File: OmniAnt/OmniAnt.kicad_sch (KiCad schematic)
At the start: 46 parts, among them J101 Connector, USB-TYPE-C-16P, J102 Conn_01x02_Pin, J103 Conn_01x04_Pin, J104 XT30PW-M, J105 XT30PW-M, J106 XT30PW-M, J107 XT30PW-M, J108 Conn_01x01, J109 Conn_01x01, J110 Conn_01x01, J111 Conn_01x01, J112 Conn_01x01, J113 Conn_01x01, J114 Conn_01x01, J115 Conn_01x01, J116 Conn_01x01, J117 Conn_01x01, U101 USBLC6-2P6, U102 TPSM53603RDA, U103 ESP32-S3-WROOM-1

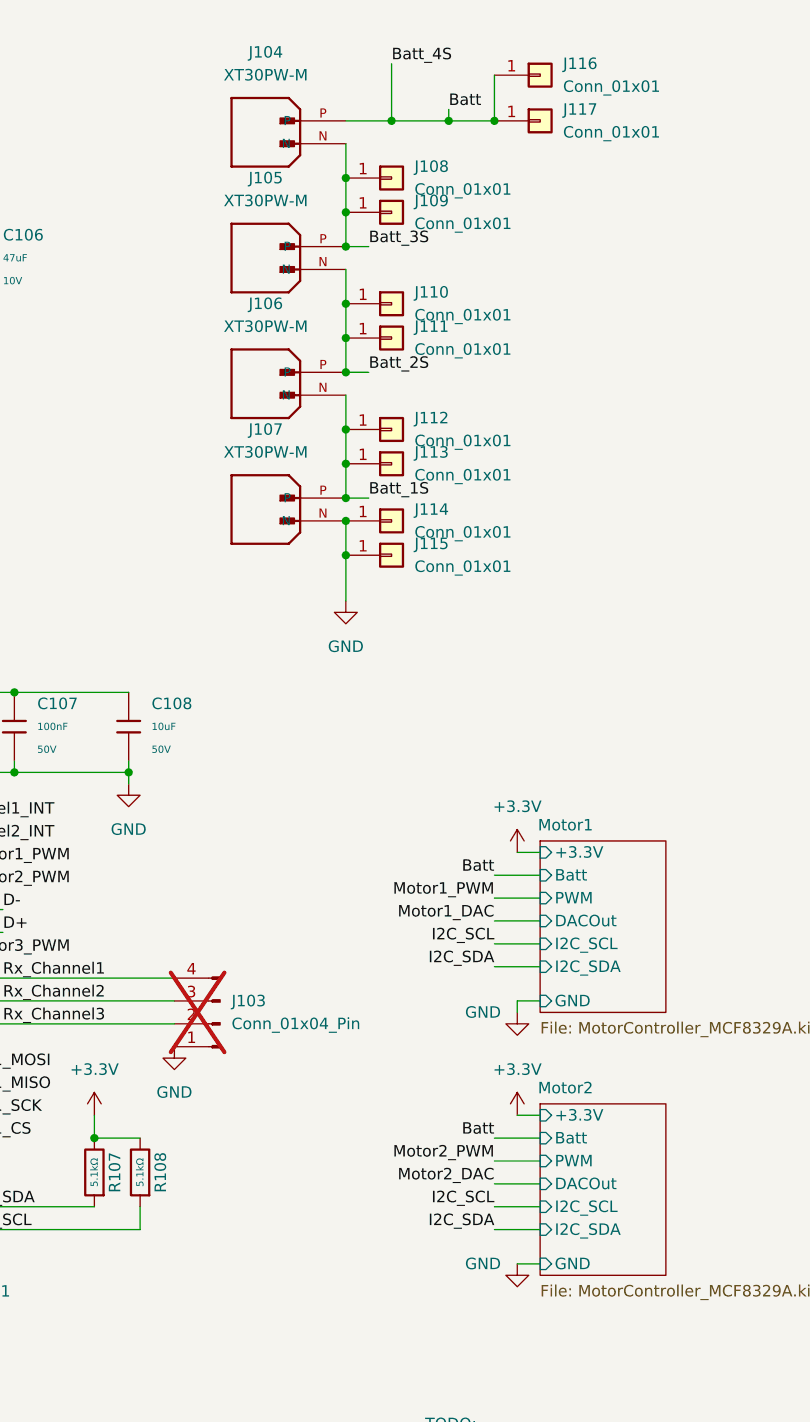
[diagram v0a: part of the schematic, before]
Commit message: I di some good work breaking out the traces around the gate driver. Unfortunatly when I went to connect the driver upto the FET array I noticed that I needed to reorder where the phase came out. To do that I needed to change the gate resistor size to make room to pull the phase through which caused a large tearup. I'm still working through it.
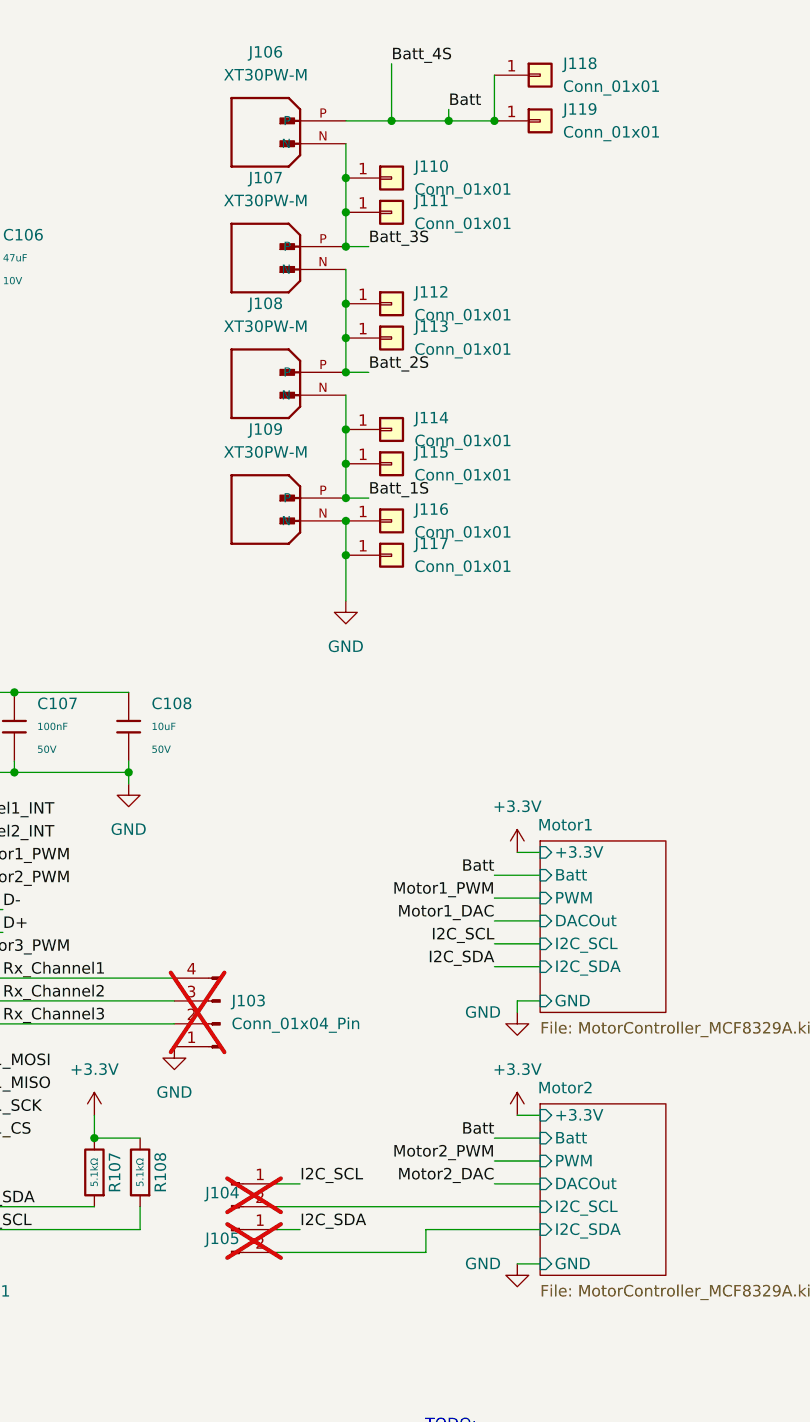
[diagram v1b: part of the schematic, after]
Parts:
- added J104, J105: Conn_01x02_Pin, Connector_PinHeader_1.27mm:PinHeader_1x02_P1.27mm_Vertical, symbol Connector:Conn_01x02_Pin
- renumbered J104 to J106, J105 to J107, J106 to J108, J107 to J109, J108 to J110, J109 to J111, J110 to J112, J111 to J113, J112 to J114, J113 to J115, J114 to J116, J115 to J117, J116 to J118, J117 to J119
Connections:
- net I2C_SCL: now also J104.1 (Pin_1)
- net I2C_SDA: now also J105.1 (Pin_1)
- new net Motor2/I2C_SCL: J104.2 (Pin_2)
- new net Motor2/I2C_SDA: J105.2 (Pin_2)
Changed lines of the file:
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@@
 	(wire
 		(pts
+			(xy 222.25 149.86) (xy 234.95 149.86)
+		)
+		(stroke
+			(width 0)
+			(type default)
+		)
+	)
+	(wire
+		(pts
 			(xy 135.89 157.48) (xy 140.97 157.48)
 		)
@@
 	(wire
 		(pts
+			(xy 222.25 152.4) (xy 222.25 149.86)
+		)
+		(stroke
+			(width 0)
+			(type default)
+		)
+	)
+	(wire
+		(pts
 			(xy 171.45 147.32) (xy 185.42 147.32)
 		)
@@
 	(wire
 		(pts
+			(xy 205.74 144.78) (xy 208.28 144.78)
+		)
+		(stroke
+			(width 0)
+			(type default)
+		)
+	)
+	(wire
+		(pts
 			(xy 213.36 26.67) (xy 218.44 26.67)
 		)
@@
 	(wire
 		(pts
-			(xy 229.87 149.86) (xy 234.95 149.86)
-		)
-		(stroke
-			(width 0)
-			(type default)
-		)
-	)
-	(wire
-		(pts
 			(xy 213.36 29.21) (xy 213.36 33.02)
 		)
@@
 	(wire
 		(pts
-			(xy 229.87 147.32) (xy 234.95 147.32)
-		)
-		(stroke
-			(width 0)
-			(type default)
-		)
-	)
-	(wire
-		(pts
 			(xy 110.49 33.02) (xy 118.11 33.02)
 		)
@@
 	(wire
 		(pts
+			(xy 205.74 149.86) (xy 208.28 149.86)
+		)
+		(stroke
+			(width 0)
+			(type default)
+		)
+	)
+	(wire
+		(pts
 			(xy 85.09 38.1) (xy 81.28 38.1)
 		)
@@
 	(wire
 		(pts
+			(xy 205.74 152.4) (xy 222.25 152.4)
+		)
+		(stroke
+			(width 0)
+			(type default)
+		)
+	)
+	(wire
+		(pts
 			(xy 229.87 142.24) (xy 234.95 142.24)
 		)
@@
 	(wire
 		(pts
+			(xy 205.74 147.32) (xy 234.95 147.32)
+		)
+		(stroke
+			(width 0)
+			(type default)
+		)
+	)
+	(wire
+		(pts
 			(xy 49.53 142.24) (xy 53.34 142.24)
 		)
@@
 	)
 	(label "I2C_SCL"
-		(at 229.87 147.32 180)
+		(at 208.28 144.78 0)
 		(effects
 			(font
 				(size 1.27 1.27)
 			)
-			(justify right bottom)
+			(justify left bottom)
 		)
 	)
@@
 	)
 	(label "I2C_SDA"
-		(at 229.87 149.86 180)
+		(at 208.28 149.86 0)
 		(effects
 			(font
 				(size 1.27 1.27)
 			)
-			(justify right bottom)
+			(justify left bottom)
 		)
 	)
@@
 		(dnp no)
 		(fields_autoplaced yes)
-		(property "Reference" "J108"
+		(property "Reference" "J110"
 			(at 220.98 31.7499 0)
 			(effects
@@
 			(project ""
 				(path "/af956454-8f11-4118-89f4-dd7ed925536a"
-					(reference "J108")
+					(reference "J110")
 					(unit 1)
 				)
@@
 		(dnp no)
 		(fields_autoplaced yes)
-		(property "Reference" "J115"
+		(property "Reference" "J117"
 			(at 220.98 73.6599 0)
 			(effects
@@
 			(project ""
 				(path "/af956454-8f11-4118-89f4-dd7ed925536a"
-					(reference "J115")
+					(reference "J117")
 					(unit 1)
 				)
@@
 		(dnp no)
 		(fields_autoplaced yes)
-		(property "Reference" "J114"
+		(property "Reference" "J116"
 			(at 220.98 69.8499 0)
 			(effects
@@
 			(project ""
 				(path "/af956454-8f11-4118-89f4-dd7ed925536a"
-					(reference "J114")
+					(reference "J116")
 					(unit 1)
 				)
@@
 	)
 	(symbol
+		(lib_id "Connector:Conn_01x02_Pin")
+		(at 200.66 144.78 0)
+		(unit 1)
+		(exclude_from_sim no)
+		(in_bom yes)
+		(on_board yes)
+		(dnp yes)
+		(property "Reference" "J104"
+			(at 199.644 145.796 0)
+			(effects
+				(font
+					(size 1.27 1.27)
+				)
+			)
+		)
+		(property "Value" "Conn_01x02_Pin"
+			(at 202.438 142.24 0)
+			(effects
+				(font
+					(size 1.27 1.27)
+				)
+				(hide yes)
+			)
+		)
+		(property "Footprint" "Connector_PinHeader_1.27mm:PinHeader_1x02_P1.27mm_Vertical"
+			(at 200.66 144.78 0)
+			(effects
+				(font
+					(size 1.27 1.27)
+				)
+				(hide yes)
+			)
+		)
+		(property "Datasheet" "~"
+			(at 200.66 144.78 0)
+			(effects
+				(font
+					(size 1.27 1.27)
+				)
+				(hide yes)
+			)
+		)
+		(property "Description" "Generic connector, single row, 01x02, script generated"
+			(at 200.66 144.78 0)
+			(effects
+				(font
+					(size 1.27 1.27)
+				)
+				(hide yes)
+			)
+		)
+		(pin "2"
+		)
+		(pin "1"
+		)
+		(instances
+			(project "OmniAnt"
+				(path "/af956454-8f11-4118-89f4-dd7ed925536a"
+					(reference "J104")
+					(unit 1)
+				)
+			)
+		)
+	)
+	(symbol
 		(lib_id "power:+3.3V")
 		(at 232.41 107.95 0)
@@
 		(dnp no)
 		(fields_autoplaced yes)
-		(property "Reference" "J113"
+		(property "Reference" "J115"
 			(at 220.98 63.4999 0)
 			(effects
@@
 			(project ""
 				(path "/af956454-8f11-4118-89f4-dd7ed925536a"
-					(reference "J113")
+					(reference "J115")
 					(unit 1)
 				)
@@
 		(dnp no)
 		(fields_autoplaced yes)
-		(property "Reference" "J107"
+		(property "Reference" "J109"
 			(at 204.47 60.96 0)
 			(effects
@@
 			(project "OmniAnt"
 				(path "/af956454-8f11-4118-89f4-dd7ed925536a"
-					(reference "J107")
+					(reference "J109")
 					(unit 1)
 				)
@@
 		(dnp no)
 		(fields_autoplaced yes)
-		(property "Reference" "J110"
+		(property "Reference" "J112"
 			(at 220.98 45.7199 0)
 			(effects
@@
 			(project ""
 				(path "/af956454-8f11-4118-89f4-dd7ed925536a"
-					(reference "J110")
+					(reference "J112")
 					(unit 1)
 				)
@@
 		(dnp no)
 		(fields_autoplaced yes)
-		(property "Reference" "J117"
+		(property "Reference" "J119"
 			(at 237.49 25.3999 0)
 			(effects
@@
 			(project ""
 				(path "/af956454-8f11-4118-89f4-dd7ed925536a"
-					(reference "J117")
+					(reference "J119")
 					(unit 1)
 				)
@@
 		(dnp no)
 		(fields_autoplaced yes)
-		(property "Reference" "J104"
+		(property "Reference" "J106"
 			(at 204.47 19.05 0)
 			(effects
@@
 			(project ""
 				(path "/af956454-8f11-4118-89f4-dd7ed925536a"
-					(reference "J104")
+					(reference "J106")
 					(unit 1)
 				)
@@
 		(dnp no)
 		(fields_autoplaced yes)
-		(property "Reference" "J105"
+		(property "Reference" "J107"
 			(at 204.47 33.02 0)
 			(effects
@@
 			(project "OmniAnt"
 				(path "/af956454-8f11-4118-89f4-dd7ed925536a"
-					(reference "J105")
+					(reference "J107")
 					(unit 1)
 				)
@@
 		(dnp no)
 		(fields_autoplaced yes)
-		(property "Reference" "J116"
+		(property "Reference" "J118"
 			(at 237.49 20.3199 0)
 			(effects
@@
 			(project ""
 				(path "/af956454-8f11-4118-89f4-dd7ed925536a"
-					(reference "J116")
+					(reference "J118")
 					(unit 1)
 				)
@@
 		(dnp no)
 		(fields_autoplaced yes)
-		(property "Reference" "J106"
+		(property "Reference" "J108"
 			(at 204.47 46.99 0)
 			(effects
@@
 			(project "OmniAnt"
 				(path "/af956454-8f11-4118-89f4-dd7ed925536a"
-					(reference "J106")
+					(reference "J108")
 					(unit 1)
 				)
@@
 		(dnp no)
 		(fields_autoplaced yes)
-		(property "Reference" "J112"
+		(property "Reference" "J114"
 			(at 220.98 59.6899 0)
 			(effects
@@
 			(project ""
 				(path "/af956454-8f11-4118-89f4-dd7ed925536a"
-					(reference "J112")
+					(reference "J114")
 					(unit 1)
 				)
@@
 		(dnp no)
 		(fields_autoplaced yes)
-		(property "Reference" "J109"
+		(property "Reference" "J111"
 			(at 220.98 35.5599 0)
 			(effects
@@
 			(project ""
 				(path "/af956454-8f11-4118-89f4-dd7ed925536a"
-					(reference "J109")
+					(reference "J111")
 					(unit 1)
 				)
@@
 	)
 	(symbol
+		(lib_id "Connector:Conn_01x02_Pin")
+		(at 200.66 149.86 0)
+		(unit 1)
+		(exclude_from_sim no)
+		(in_bom yes)
+		(on_board yes)
+		(dnp yes)
+		(property "Reference" "J105"
+			(at 199.644 150.876 0)
+			(effects
+				(font
+					(size 1.27 1.27)
+				)
+			)
+		)
+		(property "Value" "Conn_01x02_Pin"
+			(at 202.184 154.432 0)
+			(effects
+				(font
+					(size 1.27 1.27)
+				)
+				(hide yes)
+			)
+		)
+		(property "Footprint" "Connector_PinHeader_1.27mm:PinHeader_1x02_P1.27mm_Vertical"
+			(at 200.66 149.86 0)
+			(effects
+				(font
+					(size 1.27 1.27)
+				)
+				(hide yes)
+			)
+		)
+		(property "Datasheet" "~"
+			(at 200.66 149.86 0)
+			(effects
+				(font
+					(size 1.27 1.27)
+				)
+				(hide yes)
+			)
+		)
+		(property "Description" "Generic connector, single row, 01x02, script generated"
+			(at 200.66 149.86 0)
+			(effects
+				(font
+					(size 1.27 1.27)
+				)
+				(hide yes)
+			)
+		)
+		(pin "2"
+		)
+		(pin "1"
+		)
+		(instances
+			(project "OmniAnt"
+				(path "/af956454-8f11-4118-89f4-dd7ed925536a"
+					(reference "J105")
+					(unit 1)
+				)
+			)
+		)
+	)
+	(symbol
 		(lib_id "Connector_Generic:Conn_01x01")
 		(at 218.44 50.8 0)
@@
 		(dnp no)
 		(fields_autoplaced yes)
-		(property "Reference" "J111"
+		(property "Reference" "J113"
 			(at 220.98 49.5299 0)
 			(effects
@@
 			(project ""
 				(path "/af956454-8f11-4118-89f4-dd7ed925536a"
-					(reference "J111")
+					(reference "J113")
 					(unit 1)
 				)

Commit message: Really good progress. I positioned everything, and ran a bunch of signals.
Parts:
- removed J101: Connector, USB-TYPE-C-16P, PCM_JLCPCB:TYPE-C-SMD_HX-TYPE-C-16PIN, symbol PCM_JLCPCB-Extended:Connector, USB-TYPE-C-16P
- removed R101, R102: 5.1kΩ, PCM_JLCPCB:R_0402, symbol PCM_JLCPCB-Resistors:0402,5.1kΩ
- added J101: USB_B_Micro, Connector_USB:USB_Micro-B_Molex-105017-0001, symbol Connector:USB_B_Micro
- renumbered R103 to R101, R104 to R102, R105 to R103, R106 to R104, R107 to R105, R108 to R106
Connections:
- net D+: now also U101.1 (I/O1); no longer U101.3 (I/O2)
- net D-: now also U101.3 (I/O2); no longer U101.1 (I/O1)
- net GND: now also J101.4 (ID), J101.5 (GND), J101.6 (Shield)
- net VUSB: now also J101.1 (VBUS)
- net USB_D-: now reaches U101.4 (I/O2)
- net USB_D-: now also J101.2 (D-)
- net USB_D+: now reaches U101.6 (I/O1)
- net USB_D+: now also J101.3 (D+)
- no-connect marks 17 -> 15
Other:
- moved on the sheet: C101

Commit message: Everything looks good to me. I'm going to run design checks now. I'm sure it is going to be bad.
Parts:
- added H106, H107: MountingHole, MountingHole:MountingHole_3mm, symbol Mechanical:MountingHole
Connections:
- net I2C_SCL: now also R105.1, U103.24 (IO47); no longer R106.1, U103.25 (IO48)
- net I2C_SDA: now also R106.1, U103.25 (IO48); no longer R105.1, U103.24 (IO47)
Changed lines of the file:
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@@
 		)
 	)
-	(label "I2C_SCL"
+	(label "I2C_SDA"
 		(at 171.45 149.86 0)
 		(effects
@@
 		)
 	)
-	(label "I2C_SDA"
+	(label "I2C_SCL"
 		(at 171.45 147.32 0)
 		(effects
@@
 	)
 	(symbol
+		(lib_id "Mechanical:MountingHole")
+		(at 78.74 181.61 0)
+		(unit 1)
+		(exclude_from_sim no)
+		(in_bom no)
+		(on_board yes)
+		(dnp no)
+		(fields_autoplaced yes)
+		(property "Reference" "H107"
+			(at 81.28 180.3399 0)
+			(effects
+				(font
+					(size 1.27 1.27)
+				)
+				(justify left)
+			)
+		)
+		(property "Value" "MountingHole"
+			(at 81.28 182.8799 0)
+			(effects
+				(font
+					(size 1.27 1.27)
+				)
+				(justify left)
+			)
+		)
+		(property "Footprint" "MountingHole:MountingHole_3mm"
+			(at 78.74 181.61 0)
+			(effects
+				(font
+					(size 1.27 1.27)
+				)
+				(hide yes)
+			)
+		)
+		(property "Datasheet" "~"
+			(at 78.74 181.61 0)
+			(effects
+				(font
+					(size 1.27 1.27)
+				)
+				(hide yes)
+			)
+		)
+		(property "Description" "Mounting Hole without connection"
+			(at 78.74 181.61 0)
+			(effects
+				(font
+					(size 1.27 1.27)
+				)
+				(hide yes)
+			)
+		)
+		(instances
+			(project "OmniAnt"
+				(path "/af956454-8f11-4118-89f4-dd7ed925536a"
+					(reference "H107")
+					(unit 1)
+				)
+			)
+		)
+	)
+	(symbol
 		(lib_id "PCM_JLCPCB-Diodes:Schottky,SSL34F")
 		(at 88.9 33.02 90)
@@
 					(unit 1)
 				)
+			)
+		)
+	)
+	(symbol
+		(lib_id "Mechanical:MountingHole")
+		(at 21.59 182.88 0)
+		(unit 1)
+		(exclude_from_sim no)
+		(in_bom no)
+		(on_board yes)
+		(dnp no)
+		(fields_autoplaced yes)
+		(property "Reference" "H106"
+			(at 24.13 181.6099 0)
+			(effects
+				(font
+					(size 1.27 1.27)
+				)
+				(justify left)
+			)
+		)
+		(property "Value" "MountingHole"
+			(at 24.13 184.1499 0)
+			(effects
+				(font
+					(size 1.27 1.27)
+				)
+				(justify left)
+			)
+		)
+		(property "Footprint" "MountingHole:MountingHole_3mm"
+			(at 21.59 182.88 0)
+			(effects
+				(font
+					(size 1.27 1.27)
+				)
+				(hide yes)
+			)
+		)
+		(property "Datasheet" "~"
+			(at 21.59 182.88 0)
+			(effects
+				(font
+					(size 1.27 1.27)
+				)
+				(hide yes)
+			)
+		)
+		(property "Description" "Mounting Hole without connection"
+			(at 21.59 182.88 0)
+			(effects
+				(font
+					(size 1.27 1.27)
+				)
+				(hide yes)
+			)
+		)
+		(instances
+			(project "OmniAnt"
+				(path "/af956454-8f11-4118-89f4-dd7ed925536a"
+					(reference "H106")
+					(unit 1)
+				)

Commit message: Last Commit At eMatrix.
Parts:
- D105: LCSC (none) -> C2649858
- J101: LCSC (none) -> C136000
- J106, J107, J108, J109: LCSC (none) -> C431092
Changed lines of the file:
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@@
 			)
 		)
+		(property "LCSC" "C2649858"
+			(at 163.83 93.9799 0)
+			(effects
+				(font
+					(size 1.27 1.27)
+				)
+				(hide yes)
+			)
+		)
 		(pin "2"
 		)
@@
 			)
 		)
+		(property "LCSC" "C431092"
+			(at 204.47 60.96 0)
+			(effects
+				(font
+					(size 1.27 1.27)
+				)
+				(hide yes)
+			)
+		)
 		(pin "N"
 		)
@@
 			)
 		)
+		(property "LCSC" "C431092"
+			(at 204.47 19.05 0)
+			(effects
+				(font
+					(size 1.27 1.27)
+				)
+				(hide yes)
+			)
+		)
 		(pin "N"
 		)
@@
 			)
 		)
+		(property "LCSC" "C431092"
+			(at 204.47 33.02 0)
+			(effects
+				(font
+					(size 1.27 1.27)
+				)
+				(hide yes)
+			)
+		)
 		(pin "N"
 		)
@@
 			)
 		)
+		(property "LCSC" "C431092"
+			(at 204.47 46.99 0)
+			(effects
+				(font
+					(size 1.27 1.27)
+				)
+				(hide yes)
+			)
+		)
 		(pin "N"
 		)
@@
 			(effects
 				(font
+					(size 1.27 1.27)
+				)
+				(hide yes)
+			)
+		)
+		(property "LCSC" "C136000"
+			(at 33.02 25.4 0)
+			(effects
+				(font
